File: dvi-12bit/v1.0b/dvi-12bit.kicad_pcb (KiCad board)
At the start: 4 copper layers, 40 x 40.8 mm, 33 parts, among them J1 PMOD, J2 PMOD, J3 jmp, J4 5V, J5 3v3_5v_sel, J6 HDMI_A_1.4, U1 VREG_3V3, U2 TFP410

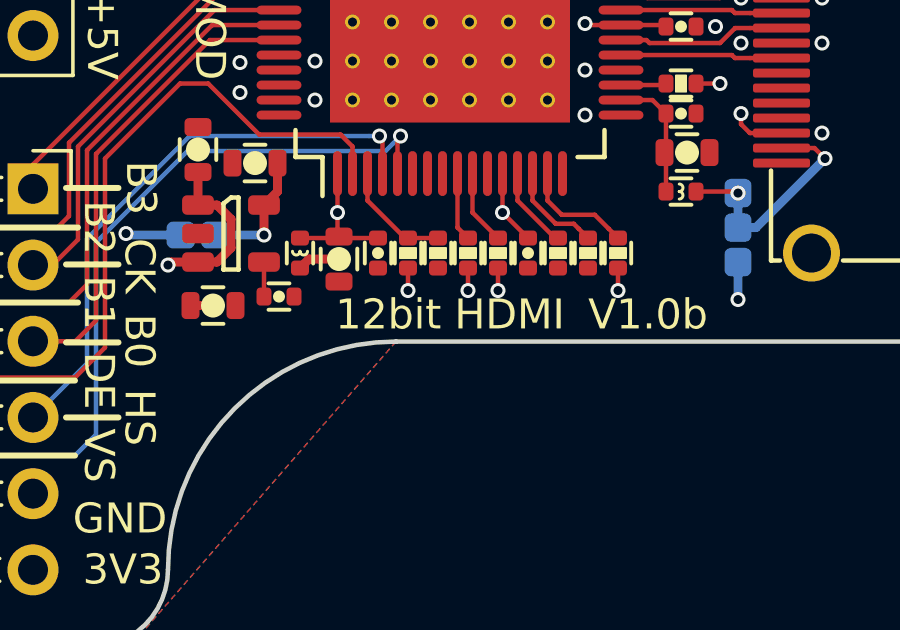
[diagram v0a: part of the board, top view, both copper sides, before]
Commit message: A few minor fixes to the dvi PMODs.
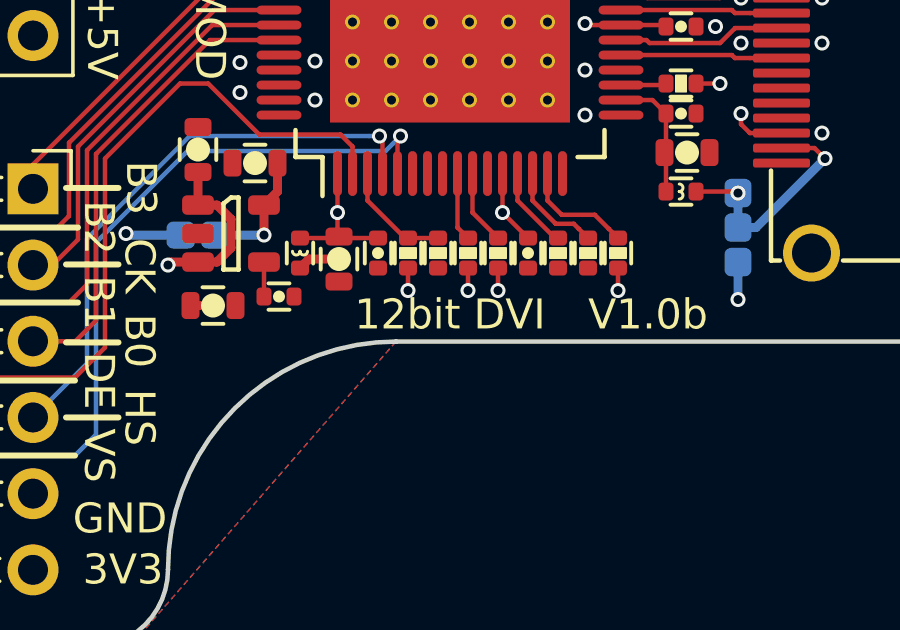
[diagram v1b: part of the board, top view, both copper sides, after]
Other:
- board text added: "12bit DVI"
- board text removed: "12bit HDMI"
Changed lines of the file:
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@@
   (gr_arc (start 31 59.6) (end 30 59.6) (angle -90) (layer Edge.Cuts) (width 0.15))
   (gr_arc (start 69 49.4) (end 69 50.4) (angle -90) (layer Edge.Cuts) (width 0.15))
-  (gr_text "12bit HDMI" (at 50.5 49.5) (layer F.SilkS)
+  (gr_text "12bit DVI" (at 50.5 49.5) (layer F.SilkS)
     (effects (font (size 1 1) (thickness 0.2)))
   )
